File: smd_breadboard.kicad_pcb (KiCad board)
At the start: 2 copper layers, 80 x 21.6 mm, 57 parts

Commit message: added caps
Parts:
- added ?: , , F.Cu at (132.1, 63.5)
- added ?: , , F.Cu at (149.9, 63.6)
- added C3: 100n, Capacitor_SMD:C_0603_1608Metric_Pad1.08x0.95mm_HandSolder, F.Cu at (156.8, 69.1)
- added C3: 100n, Capacitor_SMD:C_0603_1608Metric_Pad1.08x0.95mm_HandSolder, F.Cu at (119.1, 68.2)
- added C3: 100n, Capacitor_SMD:C_0603_1608Metric_Pad1.08x0.95mm_HandSolder, F.Cu at (179.3, 64.9)
- added C3: 100n, Capacitor_SMD:C_0603_1608Metric_Pad1.08x0.95mm_HandSolder, F.Cu at (166.8, 79.8)
- moved USB4105-GF-A 1.38 mm to (141.1, 76.5)
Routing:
- net (no net): track 427.3 -> 444.5 mm

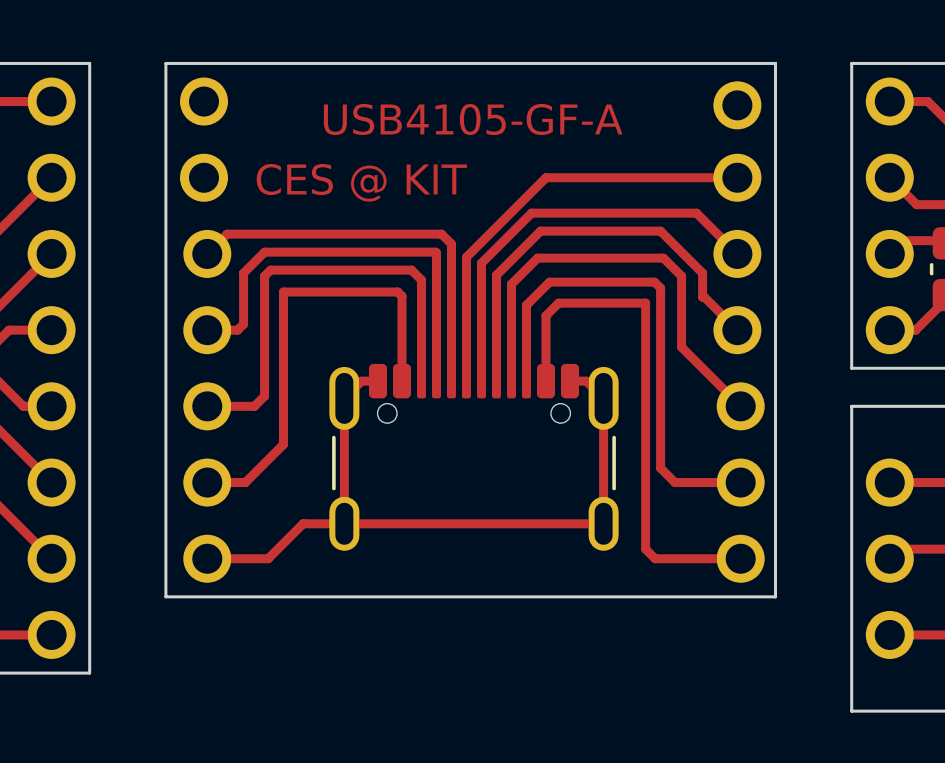
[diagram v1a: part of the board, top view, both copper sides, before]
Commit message: separated usb shield from gnd
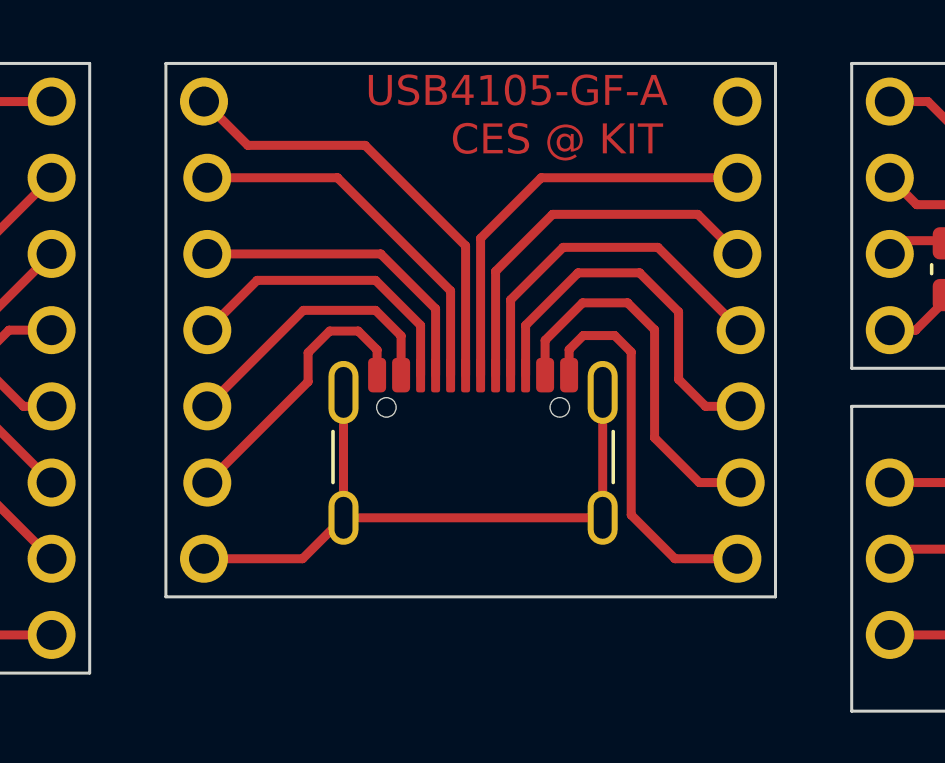
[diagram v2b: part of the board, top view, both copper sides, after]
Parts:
- removed the ? at (132.1, 63.5)
- removed the ? at (149.9, 63.6)
- added ?: , , F.Cu at (132.1, 78.7)
- added ?: , , F.Cu at (149.9, 78.7)
- moved ? 2.54 mm to (132.2, 73.7)
- moved ? 2.54 mm to (150.0, 73.7)
- moved ? 2.54 mm to (149.9, 63.5)
- moved ? 2.54 mm to (132.1, 63.5)
- moved ? 2.54 mm to (132.2, 68.6)
- moved ? 2.54 mm to (149.9, 68.6)
- moved ? 2.54 mm to (149.9, 66.0)
- moved ? 2.54 mm to (132.2, 71.1)
- moved ? 2.54 mm to (132.2, 76.2)
- moved ? 2.54 mm to (150.0, 76.2)
- moved ? 2.54 mm to (132.2, 66.0)
- moved ? 2.54 mm to (150.0, 71.1)
- moved USB4105-GF-A 0.20 mm to (141.1, 76.3)
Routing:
- net (no net): track 444.5 -> 439.2 mm

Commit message: feat: i dunno what i did?
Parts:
- moved ? 59.1 mm to (113.0, 91.4)
- moved ? 59.1 mm to (113.0, 96.5)
- moved ? 59.1 mm to (113.0, 94.0)
- moved C3 59.1 mm to (109.6, 95.0)
- moved ? 59.1 mm to (97.8, 96.5)
- moved ? 59.1 mm to (97.8, 94.0)
- moved ? 59.1 mm to (97.8, 91.4)
- moved TSOT23-6 59.1 mm to (105.0, 93.7)
- moved ? 40.5 mm to (139.7, 97.8)
- moved ? 40.5 mm to (139.7, 95.2)
- moved ? 40.5 mm to (139.7, 90.2)
- moved ? 40.5 mm to (139.7, 92.7)
- moved ? 40.5 mm to (124.5, 97.8)
- moved ? 40.5 mm to (124.5, 90.2)
- moved ? 40.5 mm to (124.5, 95.2)
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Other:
- board size 80 x 21.6 mm -> 73.7 x 36.8 mm
